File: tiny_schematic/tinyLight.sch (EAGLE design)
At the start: 37 parts, among them IC1 NCP1117, IC2 XMEGA-A4TQFP, IC3 CM1293A-02SR, J1 RASM722PX, J2 Molex, J3 PDI, Q1 BC849SMD, Q2 BC849SMD, X1 MICRO-USB

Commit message: final board (hopefully...)
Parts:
- SV1: value (none) -> RF/BT
- SV2: value (none) -> UART
- SV3: value (none) -> IR
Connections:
- removed net N$9: IC2.PC0(OC0A/SDA), SV1.4
- new net N$1: IC2.PC0(OC0A/SDA), SV1.3
- net N$8: now also SV1.4; no longer SV1.3
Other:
- moved on the sheet: SV2
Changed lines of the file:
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@@
 <?xml version="1.0" encoding="utf-8"?>
 <!DOCTYPE eagle SYSTEM "eagle.dtd">
-<eagle version="6.4">
+<eagle version="6.5.0">
 <drawing>
 <settings>
@@
 <part name="S1" library="tinyLight" deviceset="SPST_PB" device=""/>
 <part name="C9" library="rcl" deviceset="C-EU" device="C2012" value="100nF"/>
-<part name="SV1" library="con-lstb" deviceset="MA04-2" device=""/>
-<part name="SV2" library="con-lstb" deviceset="MA03-1" device=""/>
+<part name="SV1" library="con-lstb" deviceset="MA04-2" device="" value="RF/BT"/>
+<part name="SV2" library="con-lstb" deviceset="MA03-1" device="" value="UART"/>
 <part name="GND16" library="supply1" deviceset="GND" device=""/>
-<part name="SV3" library="con-lstb" deviceset="MA03-1" device=""/>
+<part name="SV3" library="con-lstb" deviceset="MA03-1" device="" value="IR"/>
 <part name="GND17" library="supply1" deviceset="GND" device=""/>
 </parts>
@@
 <instance part="C9" gate="G$1" x="25.4" y="43.18"/>
 <instance part="SV1" gate="G$1" x="48.26" y="25.4"/>
-<instance part="SV2" gate="G$1" x="185.42" y="50.8" rot="R180"/>
-<instance part="GND16" gate="1" x="175.26" y="45.72"/>
+<instance part="SV2" gate="G$1" x="187.96" y="48.26" rot="R180"/>
+<instance part="GND16" gate="1" x="177.8" y="43.18"/>
 <instance part="SV3" gate="G$1" x="81.28" y="58.42"/>
 <instance part="GND17" gate="1" x="91.44" y="53.34"/>
@@
 <pinref part="GND16" gate="1" pin="GND"/>
 <pinref part="SV2" gate="G$1" pin="3"/>
-<wire x1="175.26" y1="48.26" x2="177.8" y2="48.26" width="0.1524" layer="91"/>
+<wire x1="177.8" y1="45.72" x2="180.34" y2="45.72" width="0.1524" layer="91"/>
 </segment>
 <segment>
@@
 <segment>
 <pinref part="IC2" gate="G$1" pin="PC2(OC0C/RXD0)"/>
-<wire x1="104.14" y1="38.1" x2="60.96" y2="38.1" width="0.1524" layer="91"/>
-<wire x1="60.96" y1="38.1" x2="60.96" y2="22.86" width="0.1524" layer="91"/>
-<pinref part="SV1" gate="G$1" pin="3"/>
-<wire x1="55.88" y1="22.86" x2="60.96" y2="22.86" width="0.1524" layer="91"/>
-</segment>
-</net>
-<net name="N$9" class="0">
-<segment>
-<pinref part="IC2" gate="G$1" pin="PC0(OC0A/SDA)"/>
-<wire x1="104.14" y1="43.18" x2="33.02" y2="43.18" width="0.1524" layer="91"/>
-<wire x1="33.02" y1="43.18" x2="33.02" y2="22.86" width="0.1524" layer="91"/>
+<wire x1="104.14" y1="38.1" x2="33.02" y2="38.1" width="0.1524" layer="91"/>
+<wire x1="33.02" y1="38.1" x2="33.02" y2="22.86" width="0.1524" layer="91"/>
 <pinref part="SV1" gate="G$1" pin="4"/>
 <wire x1="33.02" y1="22.86" x2="40.64" y2="22.86" width="0.1524" layer="91"/>
@@
 <segment>
 <pinref part="IC2" gate="G$1" pin="PE3(OC0D/TXD0)"/>
-<wire x1="165.1" y1="48.26" x2="172.72" y2="48.26" width="0.1524" layer="91"/>
-<wire x1="172.72" y1="48.26" x2="172.72" y2="50.8" width="0.1524" layer="91"/>
+<wire x1="165.1" y1="48.26" x2="180.34" y2="48.26" width="0.1524" layer="91"/>
 <pinref part="SV2" gate="G$1" pin="2"/>
-<wire x1="172.72" y1="50.8" x2="177.8" y2="50.8" width="0.1524" layer="91"/>
 </segment>
 </net>
@@
 <segment>
 <pinref part="IC2" gate="G$1" pin="PE2(OC0C/RXD0)"/>
-<wire x1="165.1" y1="50.8" x2="170.18" y2="50.8" width="0.1524" layer="91"/>
-<wire x1="170.18" y1="50.8" x2="170.18" y2="53.34" width="0.1524" layer="91"/>
+<wire x1="165.1" y1="50.8" x2="180.34" y2="50.8" width="0.1524" layer="91"/>
 <pinref part="SV2" gate="G$1" pin="1"/>
-<wire x1="170.18" y1="53.34" x2="177.8" y2="53.34" width="0.1524" layer="91"/>
-</segment>
-</net>
+</segment>
+</net>
+<net name="N$1" class="0">
+<segment>
+<pinref part="IC2" gate="G$1" pin="PC0(OC0A/SDA)"/>
+<wire x1="104.14" y1="43.18" x2="58.42" y2="43.18" width="0.1524" layer="91"/>
+<wire x1="58.42" y1="43.18" x2="58.42" y2="22.86" width="0.1524" layer="91"/>
+<pinref part="SV1" gate="G$1" pin="3"/>
+<wire x1="58.42" y1="22.86" x2="55.88" y2="22.86" width="0.1524" layer="91"/>
+</segment>
+</net>

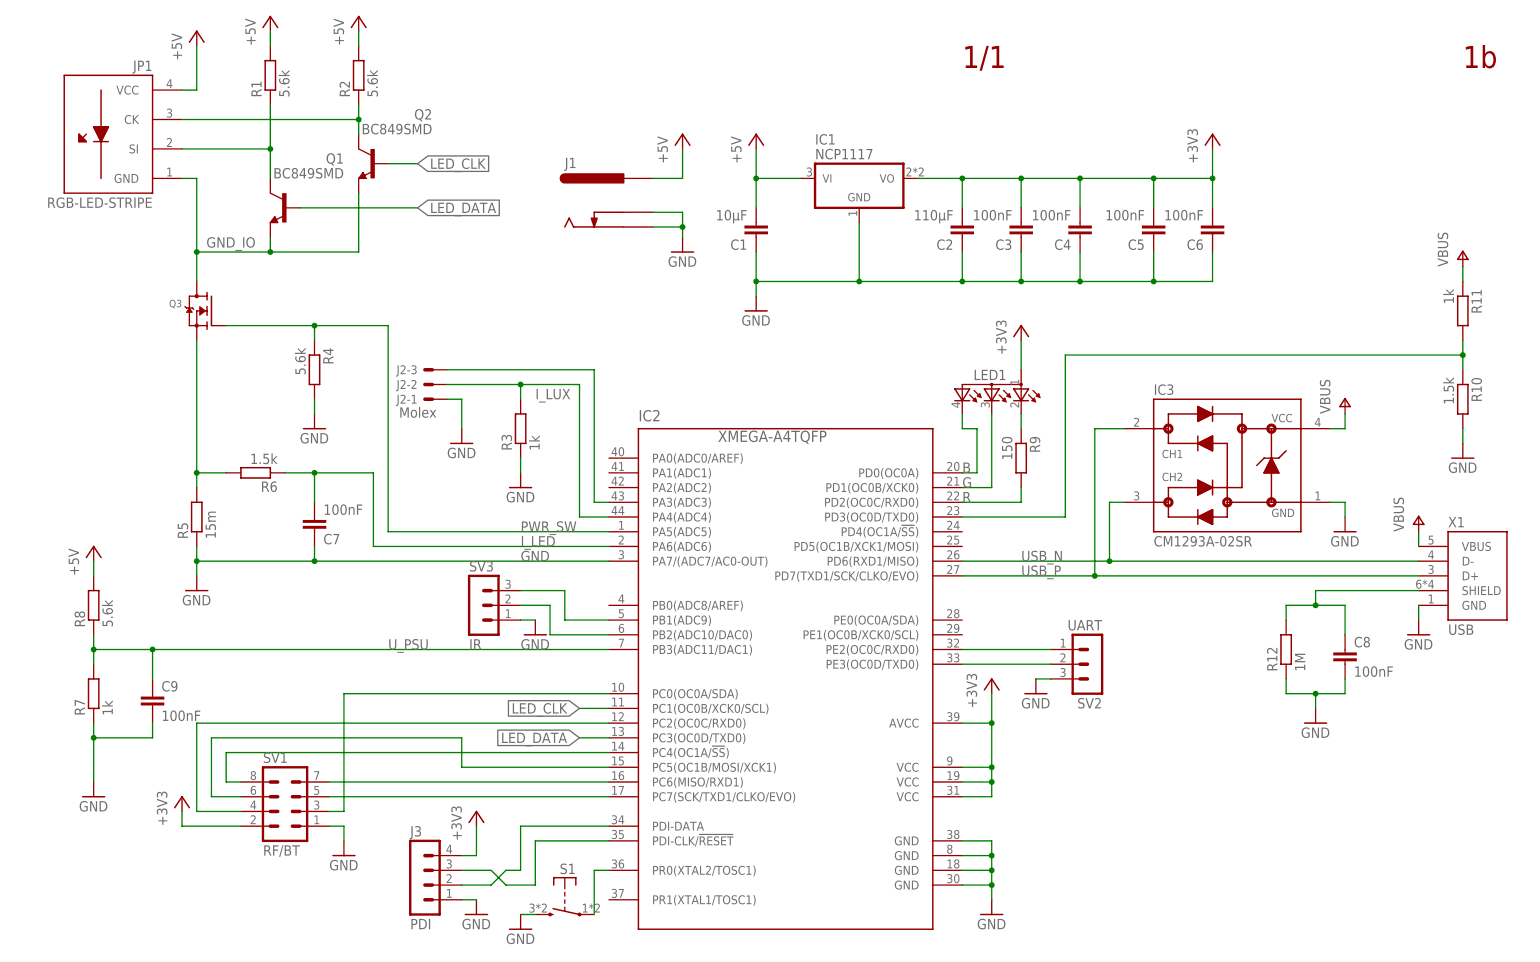
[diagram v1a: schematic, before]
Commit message: added revision reference, RF net names, fixed cap value
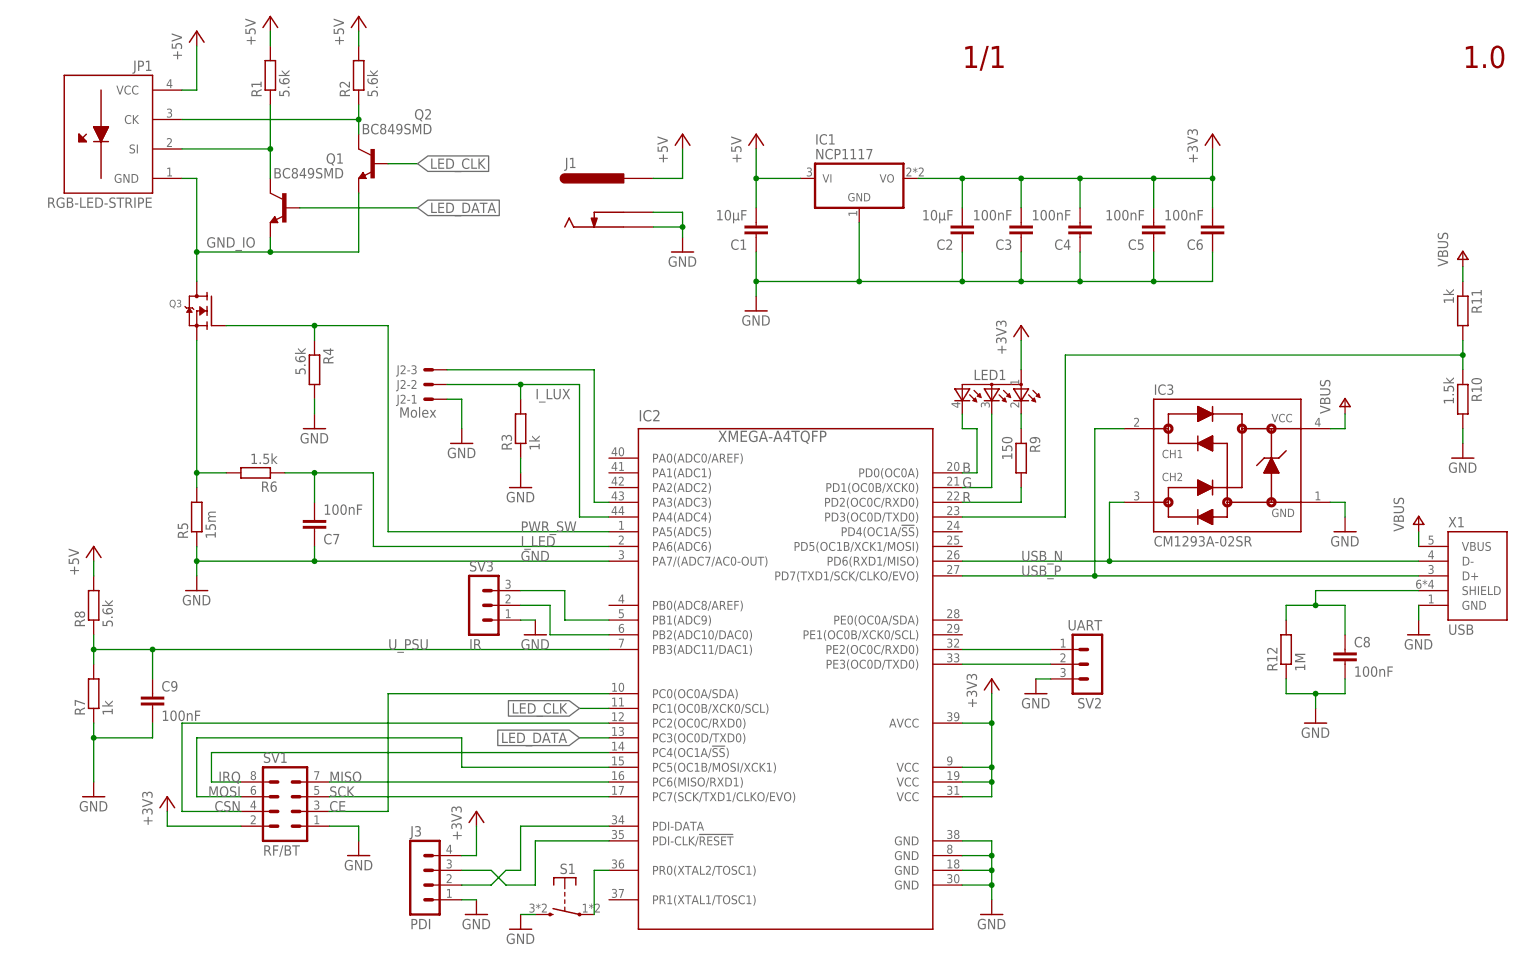
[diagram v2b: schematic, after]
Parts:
- C2: value 110µF -> 10µF
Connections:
- net N$1 renamed CE
- net N$4 renamed SCK
- net N$5 renamed MOSI
- net N$6 renamed MISO
- net N$7 renamed IRQ
- net N$8 renamed CSN
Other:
- note added: "1.0"
- note removed: "1b"
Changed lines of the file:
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@@
 <part name="GND4" library="supply1" deviceset="GND" device=""/>
 <part name="C1" library="rcl" deviceset="C-EU" device="C2012" value="10µF"/>
-<part name="C2" library="rcl" deviceset="C-EU" device="C2012" value="110µF"/>
+<part name="C2" library="rcl" deviceset="C-EU" device="C2012" value="10µF"/>
 <part name="P+1" library="supply1" deviceset="+5V" device=""/>
 <part name="GND1" library="supply1" deviceset="GND" device=""/>
@@
 <sheet>
 <plain>
-<text x="251.46" y="154.94" size="3.81" layer="94" align="top-left">1b</text>
+<text x="251.46" y="154.94" size="3.81" layer="94" align="top-left">1.0</text>
 <text x="165.1" y="154.94" size="3.81" layer="94" align="top-left">1/1</text>
 </plain>
@@
 <instance part="R12" gate="G$1" x="220.98" y="50.8" rot="R90"/>
 <instance part="C8" gate="G$1" x="231.14" y="50.8"/>
-<instance part="GND5" gate="1" x="58.42" y="15.24"/>
-<instance part="+3V5" gate="G$1" x="30.48" y="25.4"/>
+<instance part="GND5" gate="1" x="60.96" y="15.24"/>
+<instance part="+3V5" gate="G$1" x="27.94" y="25.4"/>
 <instance part="+3V6" gate="G$1" x="81.28" y="22.86"/>
 <instance part="R4" gate="G$1" x="53.34" y="99.06" rot="R270"/>
@@
 <segment>
 <pinref part="GND5" gate="1" pin="GND"/>
-<wire x1="58.42" y1="20.32" x2="58.42" y2="17.78" width="0.1524" layer="91"/>
+<wire x1="60.96" y1="20.32" x2="60.96" y2="17.78" width="0.1524" layer="91"/>
 <pinref part="SV1" gate="G$1" pin="1"/>
-<wire x1="55.88" y1="20.32" x2="58.42" y2="20.32" width="0.1524" layer="91"/>
+<wire x1="55.88" y1="20.32" x2="60.96" y2="20.32" width="0.1524" layer="91"/>
 </segment>
 <segment>
@@
 <segment>
 <pinref part="+3V5" gate="G$1" pin="+3V3"/>
-<wire x1="30.48" y1="22.86" x2="30.48" y2="20.32" width="0.1524" layer="91"/>
+<wire x1="27.94" y1="22.86" x2="27.94" y2="20.32" width="0.1524" layer="91"/>
 <pinref part="SV1" gate="G$1" pin="2"/>
-<wire x1="40.64" y1="20.32" x2="30.48" y2="20.32" width="0.1524" layer="91"/>
+<wire x1="40.64" y1="20.32" x2="27.94" y2="20.32" width="0.1524" layer="91"/>
 </segment>
 </net>
@@
 </segment>
 </net>
-<net name="N$5" class="0">
-<segment>
-<wire x1="35.56" y1="25.4" x2="35.56" y2="35.56" width="0.1524" layer="91"/>
-<wire x1="35.56" y1="35.56" x2="78.74" y2="35.56" width="0.1524" layer="91"/>
+<net name="MOSI" class="0">
+<segment>
+<wire x1="33.02" y1="25.4" x2="33.02" y2="35.56" width="0.1524" layer="91"/>
+<wire x1="33.02" y1="35.56" x2="78.74" y2="35.56" width="0.1524" layer="91"/>
 <wire x1="78.74" y1="35.56" x2="78.74" y2="30.48" width="0.1524" layer="91"/>
 <pinref part="IC2" gate="G$1" pin="PC5(OC1B/MOSI/XCK1)"/>
 <wire x1="78.74" y1="30.48" x2="104.14" y2="30.48" width="0.1524" layer="91"/>
 <pinref part="SV1" gate="G$1" pin="6"/>
-<wire x1="35.56" y1="25.4" x2="40.64" y2="25.4" width="0.1524" layer="91"/>
-</segment>
-</net>
-<net name="N$6" class="0">
+<wire x1="33.02" y1="25.4" x2="40.64" y2="25.4" width="0.1524" layer="91"/>
+<label x="40.64" y="25.4" size="1.778" layer="95" rot="MR0"/>
+</segment>
+</net>
+<net name="MISO" class="0">
 <segment>
 <pinref part="IC2" gate="G$1" pin="PC6(MISO/RXD1)"/>
 <wire x1="104.14" y1="27.94" x2="55.88" y2="27.94" width="0.1524" layer="91"/>
 <pinref part="SV1" gate="G$1" pin="7"/>
-</segment>
-</net>
-<net name="N$4" class="0">
+<label x="55.88" y="27.94" size="1.778" layer="95"/>
+</segment>
+</net>
+<net name="SCK" class="0">
 <segment>
 <pinref part="SV1" gate="G$1" pin="5"/>
 <pinref part="IC2" gate="G$1" pin="PC7(SCK/TXD1/CLKO/EVO)"/>
 <wire x1="55.88" y1="25.4" x2="104.14" y2="25.4" width="0.1524" layer="91"/>
-</segment>
-</net>
-<net name="N$7" class="0">
+<label x="55.88" y="25.4" size="1.778" layer="95"/>
+</segment>
+</net>
+<net name="IRQ" class="0">
 <segment>
 <pinref part="IC2" gate="G$1" pin="PC4(OC1A/!SS!)"/>
-<wire x1="104.14" y1="33.02" x2="38.1" y2="33.02" width="0.1524" layer="91"/>
-<wire x1="38.1" y1="33.02" x2="38.1" y2="27.94" width="0.1524" layer="91"/>
+<wire x1="104.14" y1="33.02" x2="35.56" y2="33.02" width="0.1524" layer="91"/>
+<wire x1="35.56" y1="33.02" x2="35.56" y2="27.94" width="0.1524" layer="91"/>
 <pinref part="SV1" gate="G$1" pin="8"/>
-<wire x1="38.1" y1="27.94" x2="40.64" y2="27.94" width="0.1524" layer="91"/>
-</segment>
-</net>
-<net name="N$8" class="0">
+<wire x1="35.56" y1="27.94" x2="40.64" y2="27.94" width="0.1524" layer="91"/>
+<label x="40.64" y="27.94" size="1.778" layer="95" rot="MR0"/>
+</segment>
+</net>
+<net name="CSN" class="0">
 <segment>
 <pinref part="IC2" gate="G$1" pin="PC2(OC0C/RXD0)"/>
-<wire x1="104.14" y1="38.1" x2="33.02" y2="38.1" width="0.1524" layer="91"/>
-<wire x1="33.02" y1="38.1" x2="33.02" y2="22.86" width="0.1524" layer="91"/>
+<wire x1="104.14" y1="38.1" x2="30.48" y2="38.1" width="0.1524" layer="91"/>
+<wire x1="30.48" y1="38.1" x2="30.48" y2="22.86" width="0.1524" layer="91"/>
 <pinref part="SV1" gate="G$1" pin="4"/>
-<wire x1="33.02" y1="22.86" x2="40.64" y2="22.86" width="0.1524" layer="91"/>
+<wire x1="30.48" y1="22.86" x2="40.64" y2="22.86" width="0.1524" layer="91"/>
+<label x="40.64" y="22.86" size="1.778" layer="95" rot="MR0"/>
 </segment>
 </net>
@@
 </segment>
 </net>
-<net name="N$1" class="0">
+<net name="CE" class="0">
 <segment>
 <pinref part="IC2" gate="G$1" pin="PC0(OC0A/SDA)"/>
-<wire x1="104.14" y1="43.18" x2="58.42" y2="43.18" width="0.1524" layer="91"/>
-<wire x1="58.42" y1="43.18" x2="58.42" y2="22.86" width="0.1524" layer="91"/>
+<wire x1="104.14" y1="43.18" x2="66.04" y2="43.18" width="0.1524" layer="91"/>
+<wire x1="66.04" y1="43.18" x2="66.04" y2="22.86" width="0.1524" layer="91"/>
 <pinref part="SV1" gate="G$1" pin="3"/>
-<wire x1="58.42" y1="22.86" x2="55.88" y2="22.86" width="0.1524" layer="91"/>
-</segment>
-</net>
+<wire x1="66.04" y1="22.86" x2="55.88" y2="22.86" width="0.1524" layer="91"/>
+<label x="55.88" y="22.86" size="1.778" layer="95"/>
+</segment>
+</net>

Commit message: fixed colorswirl, added settings preset, minor improvements
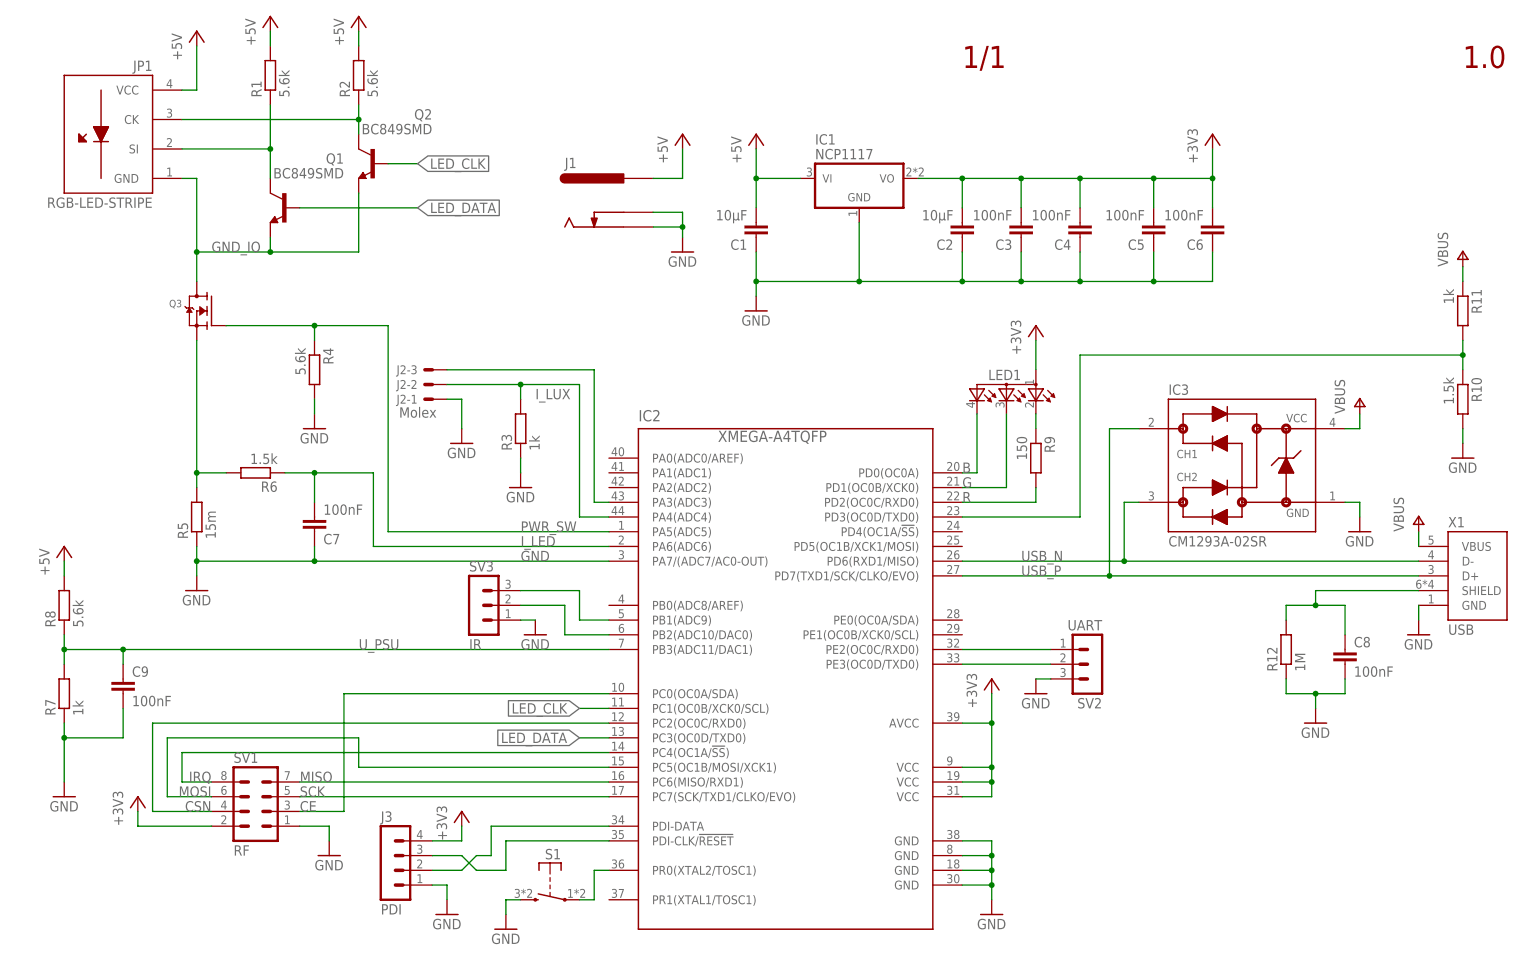
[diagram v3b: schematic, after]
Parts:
- SV1: value RF/BT -> RF
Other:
- moved on the sheet: C9, IC3, J3, LED1, R7, R8, R9, S1, SV1
